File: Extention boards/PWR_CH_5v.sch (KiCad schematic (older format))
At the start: 25 parts, among them U11 INA4180, U25 TPS22810, U26 TPS22810, U27 INA4180, U28 LM339

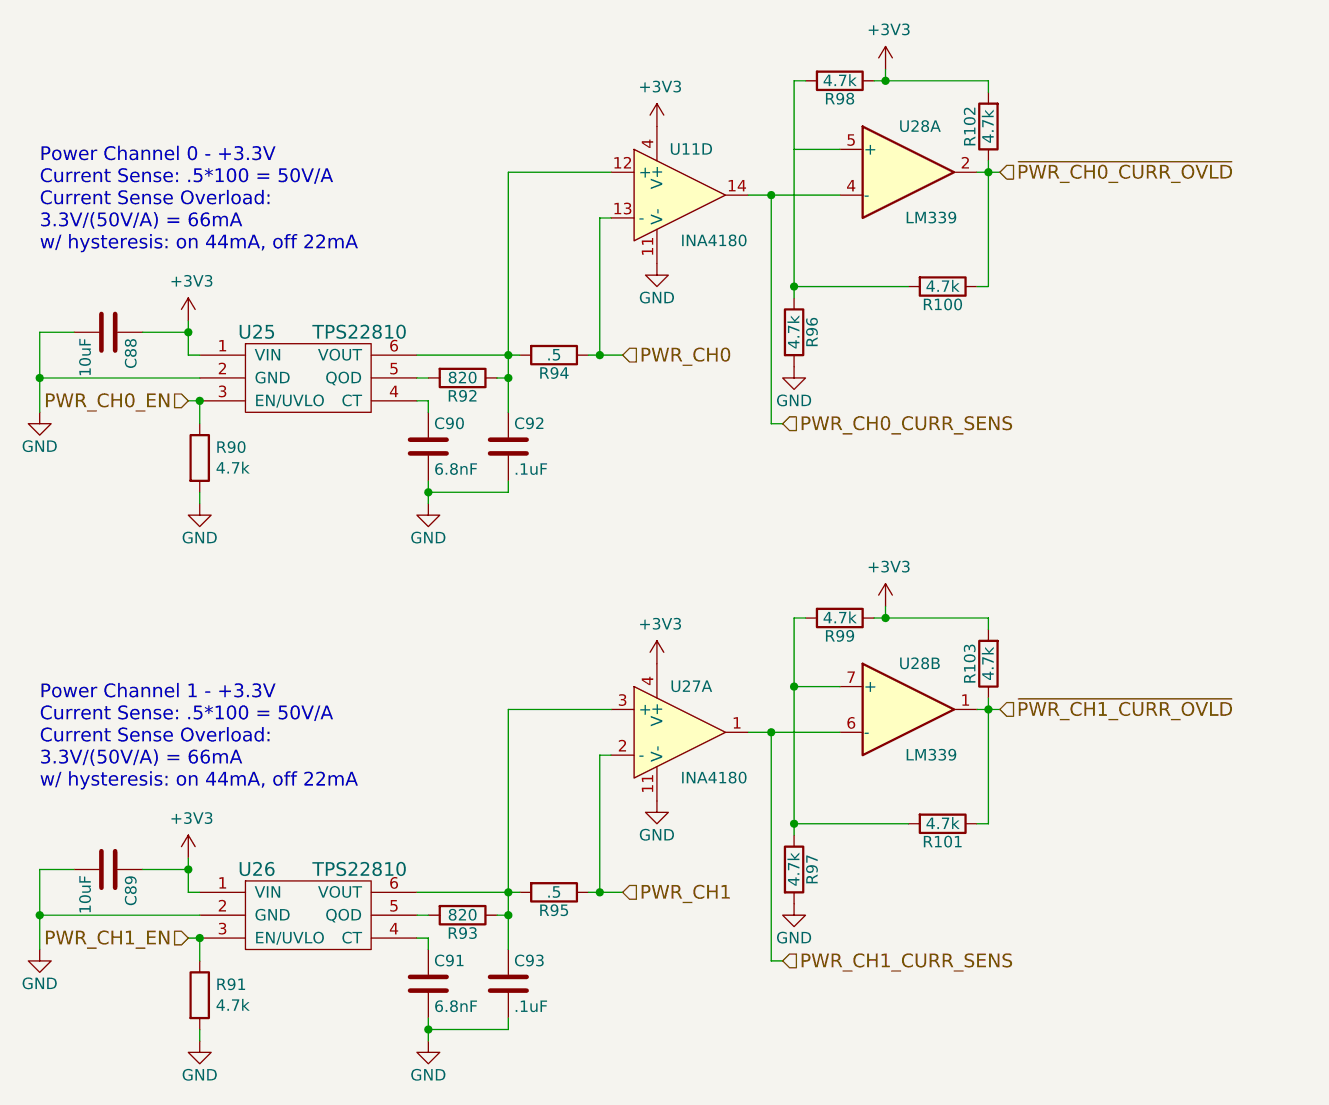
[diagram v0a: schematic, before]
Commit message: New voltage reg, better voltage protection, and consolidated component counts
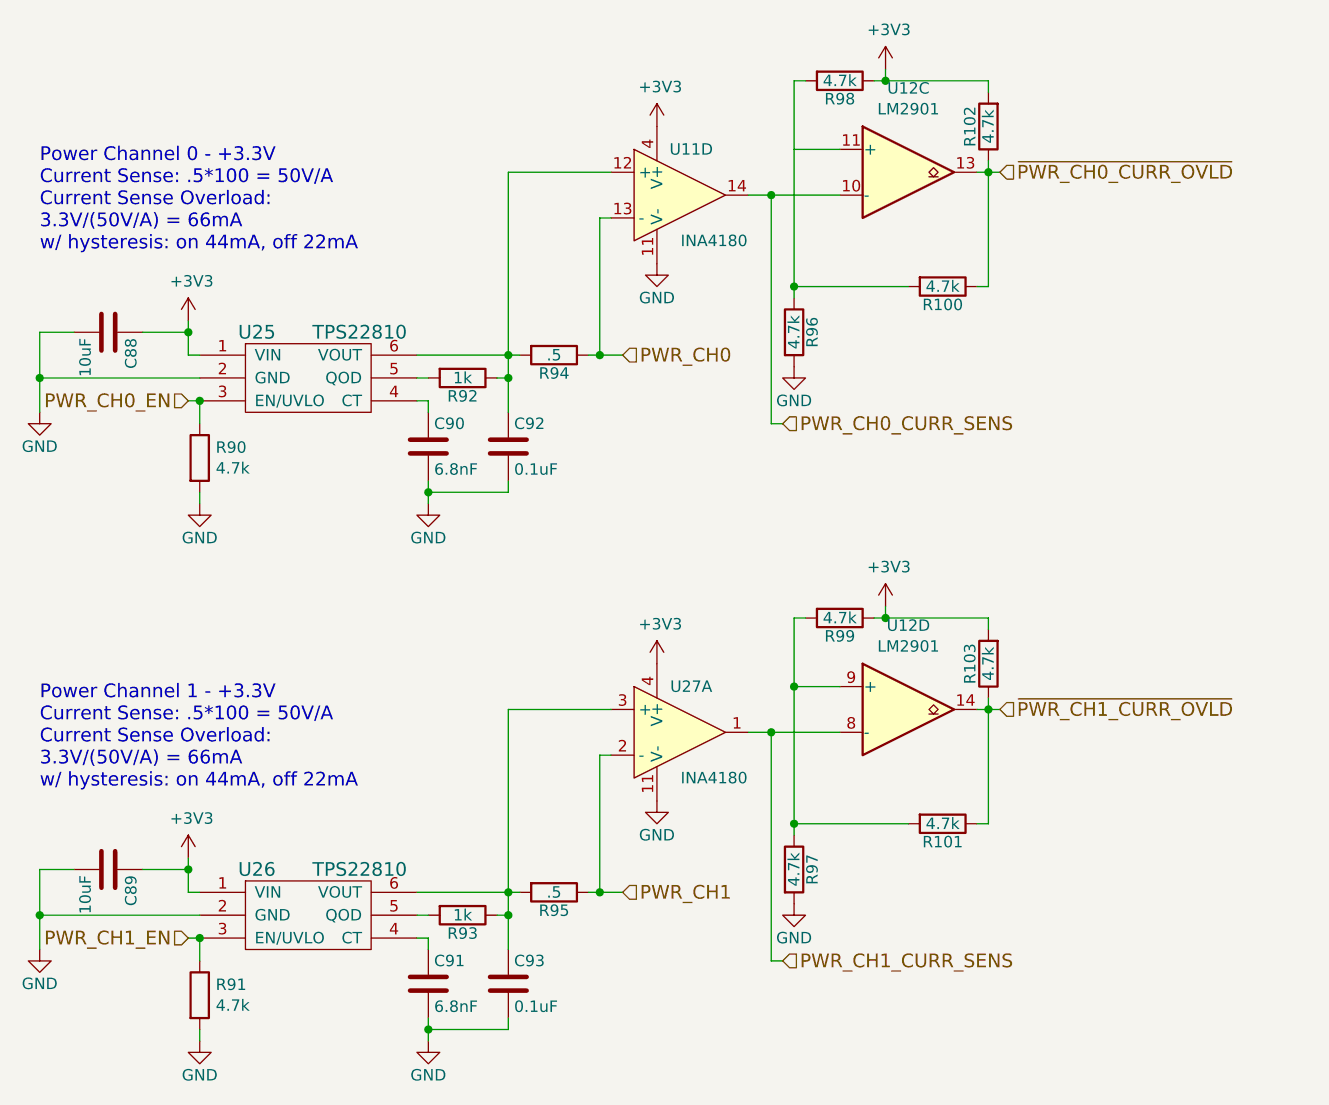
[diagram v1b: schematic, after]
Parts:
- removed U28: LM339, Package_SO:SOIC-14_3.9x8.7mm_P1.27mm, symbol Comparator:LM339
- added U12: LM2901, Package_SO:TSSOP-14_4.4x5mm_P0.65mm, symbol Comparator:LM2901
- C92, C93: value .1uF -> 0.1uF
- R92, R93: value 820 -> 1k
- U11, U27: DigiKey Part Number (none) -> 296-49096-1-ND
- U25, U26: DigiKey Part Number (none) -> 296-45297-1-ND
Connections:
- net PWR_CH0_CURR_SENS: now also U12.10 (-)
- net PWR_CH1_CURR_SENS: now also U12.8 (-)
- net ~PWR_CH0_CURR_OVLD: now also U12.13
- net ~PWR_CH1_CURR_OVLD: now also U12.14
- net at R100.2, R96.1, R98.2: now also U12.11 (+)
- net at R101.2, R97.1, R99.2: now also U12.9 (+)
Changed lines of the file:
@@
 F 2 "Package_TO_SOT_SMD:SOT-23-6_Handsoldering" H 2850 2950 60  0001 C CNN
 F 3 "" H 2850 2950 60  0000 C CNN
+F 4 "296-45297-1-ND" H 2850 2950 50  0001 C CNN "DigiKey Part Number"
 	1    2850 2950
 	1    0    0    -1
@@
 AR Path="/5D27F048/5F73E92B/5F77DD97" Ref="R92"  Part="1"
 F 0 "R92" V 3630 3350 50  0000 C CNN
-F 1 "820" V 3550 3350 50  0000 C CNN
+F 1 "1k" V 3550 3350 50  0000 C CNN
 F 2 "Resistor_SMD:R_1206_3216Metric_Pad1.42x1.75mm_HandSolder" V 3480 3350 50  0001 C CNN
 F 3 "" H 3550 3350 50  0000 C CNN
@@
 AR Path="/5D27F048/5F73E92B/5F77DDA3" Ref="C92"  Part="1"
 F 0 "C92" H 3775 3750 50  0000 L CNN
-F 1 ".1uF" H 3775 3550 50  0000 L CNN
+F 1 "0.1uF" H 3775 3550 50  0000 L CNN
 F 2 "Capacitor_SMD:C_1206_3216Metric_Pad1.42x1.75mm_HandSolder" H 3788 3500 50  0001 C CNN
 F 3 "" H 3750 3650 50  0000 C CNN
@@
 F 2 "Package_TO_SOT_SMD:SOT-23-6_Handsoldering" H 2850 5300 60  0001 C CNN
 F 3 "" H 2850 5300 60  0000 C CNN
+F 4 "296-45297-1-ND" H 2850 5300 50  0001 C CNN "DigiKey Part Number"
 	1    2850 5300
 	1    0    0    -1
@@
 AR Path="/5D27F048/5F73E92B/5F77DDD7" Ref="R93"  Part="1"
 F 0 "R93" V 3630 5700 50  0000 C CNN
-F 1 "820" V 3550 5700 50  0000 C CNN
+F 1 "1k" V 3550 5700 50  0000 C CNN
 F 2 "Resistor_SMD:R_1206_3216Metric_Pad1.42x1.75mm_HandSolder" V 3480 5700 50  0001 C CNN
 F 3 "" H 3550 5700 50  0000 C CNN
@@
 AR Path="/5D27F048/5F73E92B/5F77DDE3" Ref="C93"  Part="1"
 F 0 "C93" H 3775 6100 50  0000 L CNN
-F 1 ".1uF" H 3775 5900 50  0000 L CNN
+F 1 "0.1uF" H 3775 5900 50  0000 L CNN
 F 2 "Capacitor_SMD:C_1206_3216Metric_Pad1.42x1.75mm_HandSolder" H 3788 5850 50  0001 C CNN
 F 3 "" H 3750 6000 50  0000 C CNN
@@
 F 2 "Package_SO:TSSOP-14_4.4x5mm_P0.65mm" H 4450 5000 50  0001 C CNN
 F 3 "" H 4550 5100 50  0000 C CNN
+F 4 "296-49096-1-ND" H 4500 4900 50  0001 C CNN "DigiKey Part Number"
 	1    4500 4900
 	1    0    0    -1
@@
 Connection ~ 4150 5600
 $Comp
-L Comparator:LM339 U?
-U 1 1 5F77DE45
-P 5500 2450
-AR Path="/5D27F048/5D65270B/5F77DE45" Ref="U?"  Part="1"
-AR Path="/5D27F048/5F73E92B/5F77DE45" Ref="U28"  Part="1"
-F 0 "U28" H 5550 2650 50  0000 C CNN
-F 1 "LM339" H 5600 2250 50  0000 C CNN
-F 2 "Package_SO:SOIC-14_3.9x8.7mm_P1.27mm" H 5450 2550 50  0001 C CNN
-F 3 "" H 5550 2650 50  0000 C CNN
-	1    5500 2450
-	1    0    0    -1
-$EndComp
-$Comp
 L Device:R R?
 U 1 1 5F77DE4B
@@
 Wire Wire Line
 	4900 3550 4950 3550
-$Comp
-L Comparator:LM339 U?
-U 2 1 5F77DE68
-P 5500 4800
-AR Path="/5D27F048/5D65270B/5F77DE68" Ref="U?"  Part="2"
-AR Path="/5D27F048/5F73E92B/5F77DE68" Ref="U28"  Part="2"
-F 0 "U28" H 5550 5000 50  0000 C CNN
-F 1 "LM339" H 5600 4600 50  0000 C CNN
-F 2 "Package_SO:SOIC-14_3.9x8.7mm_P1.27mm" H 5450 4900 50  0001 C CNN
-F 3 "" H 5550 5000 50  0000 C CNN
-	2    5500 4800
-	1    0    0    -1
-$EndComp
 $Comp
 L Device:R R?
@@
 F 2 "Package_SO:TSSOP-14_4.4x5mm_P0.65mm" H 4450 2650 50  0001 C CNN
 F 3 "" H 4550 2750 50  0000 C CNN
+F 4 "296-49096-1-ND" H 4500 2550 50  0001 C CNN "DigiKey Part Number"
 	4    4500 2550
 	1    0    0    -1
 $EndComp
 Connection ~ 5000 4700
+$Comp
+L Comparator:LM2901 U12
+U 3 1 5F9AF0BC
+P 5500 2450
+F 0 "U12" H 5500 2817 50  0000 C CNN
+F 1 "LM2901" H 5500 2726 50  0000 C CNN
+F 2 "Package_SO:TSSOP-14_4.4x5mm_P0.65mm" H 5450 2550 50  0001 C CNN
+F 3 "https://www.st.com/resource/en/datasheet/lm2901.pdf" H 5550 2650 50  0001 C CNN
+F 4 "296-41294-1-ND" H 5500 2450 50  0001 C CNN "DigiKey Part Number"
+	3    5500 2450
+	1    0    0    -1
+$EndComp
+$Comp
+L Comparator:LM2901 U12
+U 4 1 5F9B053D
+P 5500 4800
+F 0 "U12" H 5500 5167 50  0000 C CNN
+F 1 "LM2901" H 5500 5076 50  0000 C CNN
+F 2 "Package_SO:TSSOP-14_4.4x5mm_P0.65mm" H 5450 4900 50  0001 C CNN
+F 3 "https://www.st.com/resource/en/datasheet/lm2901.pdf" H 5550 5000 50  0001 C CNN
+F 4 "296-41294-1-ND" H 5500 4800 50  0001 C CNN "DigiKey Part Number"
+	4    5500 4800
+	1    0    0    -1
+$EndComp
 $EndSCHEMATC
